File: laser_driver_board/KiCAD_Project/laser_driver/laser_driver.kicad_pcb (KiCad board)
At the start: 2 copper layers, 101.6 x 33 mm, 9 parts, among them J1 Input, J2 Output, U1 LD1255R

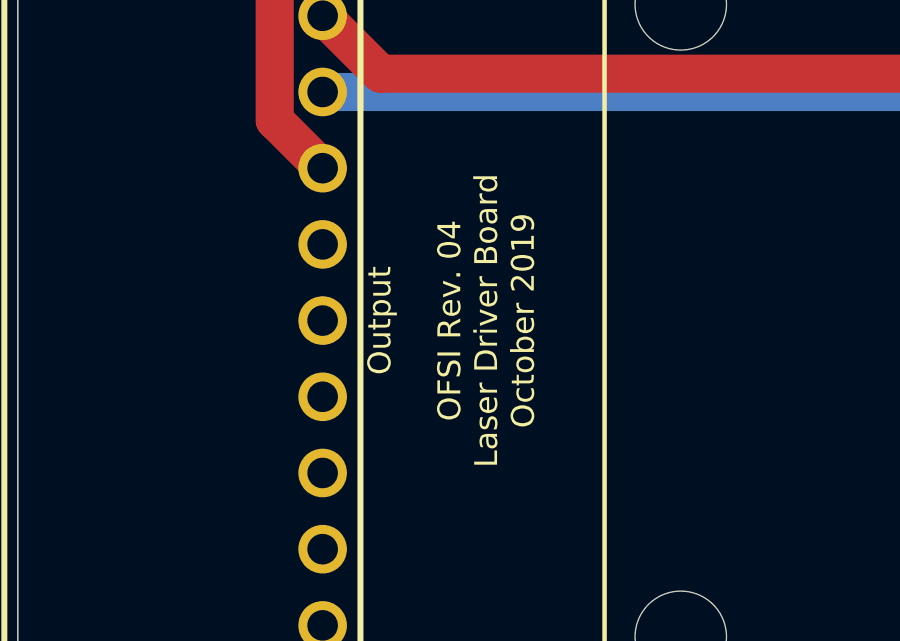
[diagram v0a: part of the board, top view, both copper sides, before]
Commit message: Change laser driver to OFMI
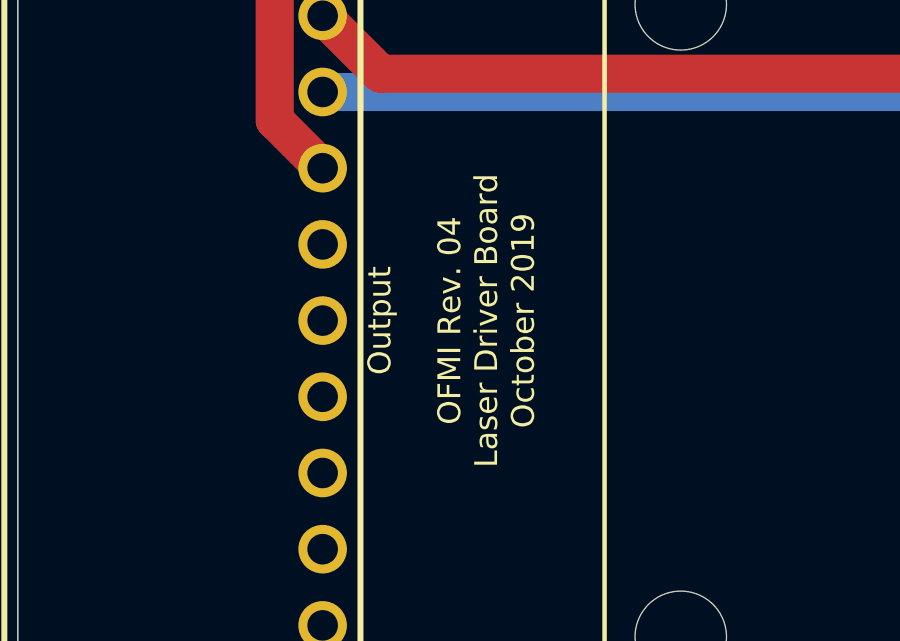
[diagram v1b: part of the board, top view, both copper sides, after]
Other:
- board text added: "OFMI Rev. 04 Laser Driver Board October 2019"
- board text removed: "OFSI Rev. 04 Laser Driver Board October 2019"
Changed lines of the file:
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@@
     (effects (font (size 0.762 0.762) (thickness 0.15)) (justify mirror))
   )
-  (gr_text "OFSI Rev. 04\nLaser Driver Board\nOctober 2019" (at 142.621 92.71 90) (layer F.SilkS)
+  (gr_text "OFMI Rev. 04\nLaser Driver Board\nOctober 2019" (at 142.621 92.71 90) (layer F.SilkS)
     (effects (font (size 0.762 0.762) (thickness 0.15)))
   )

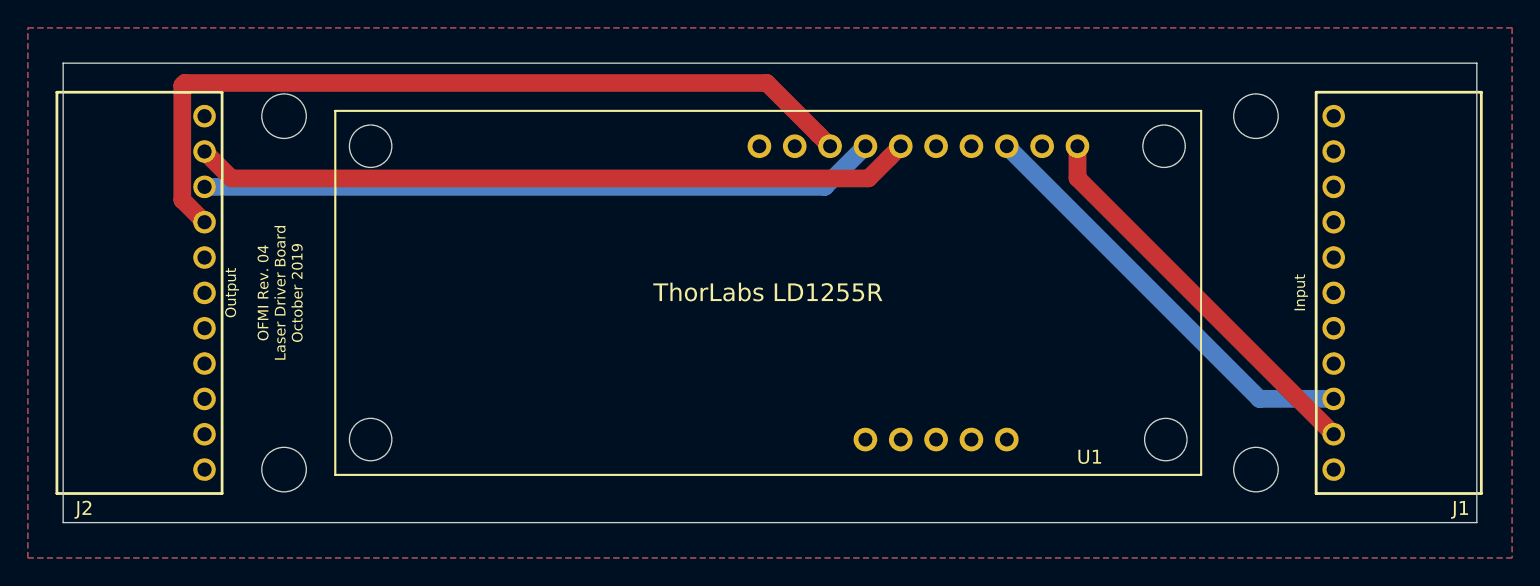
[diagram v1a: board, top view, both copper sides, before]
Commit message: Laser driver board rev 4.1 updates.
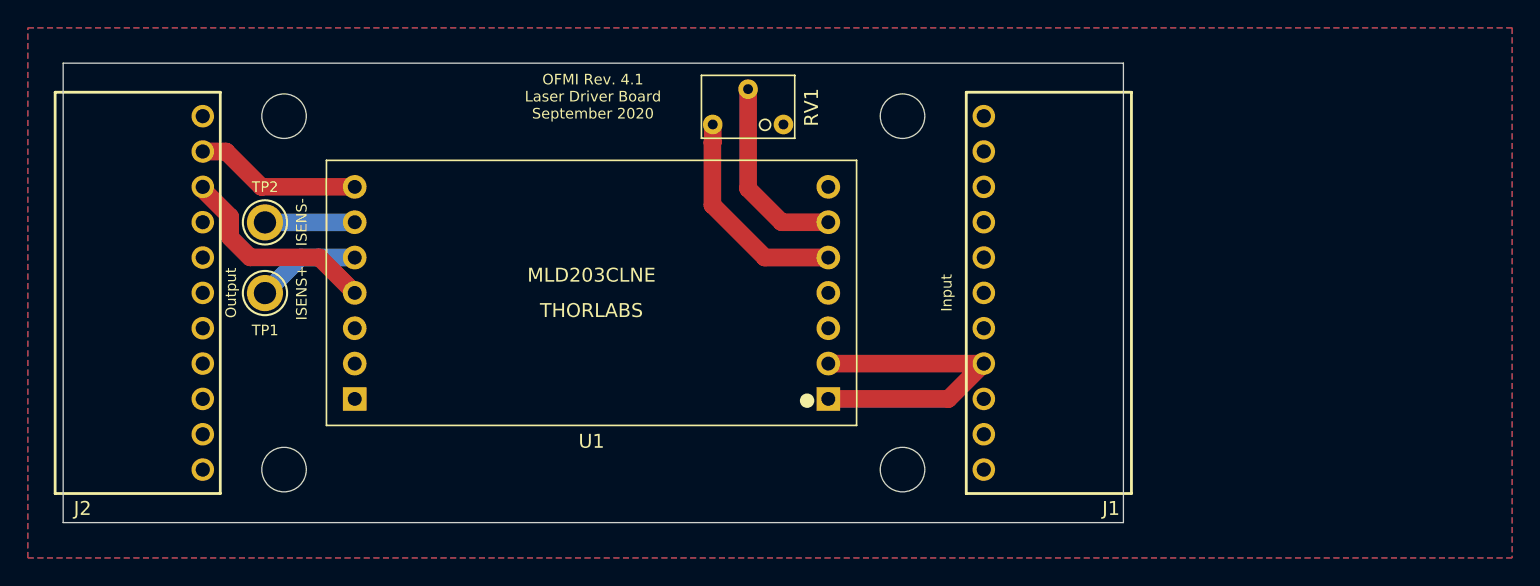
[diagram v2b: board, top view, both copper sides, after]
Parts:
- removed OB1, OB2: Test Point (on LD1255R), lib_fp:OffBoard
- added RV1: R_POT, lib_fp:3266W, F.Cu at (176.2, 79.3)
- added TP1: TestPoint, lib_fp:5006_TestPoint, F.Cu at (141.5, 92.7)
- added TP2: TestPoint, lib_fp:5006_TestPoint, F.Cu at (141.5, 87.6)
- U1: value LD1255R -> MLD203CLNE; footprint lib_fp:LD1255R -> lib_fp:MLD203CLN
- moved H3 25.4 mm to (187.3, 80.0)
- moved H4 25.4 mm to (187.3, 105.4)
- moved J1 25.1 mm to (196.2, 92.7)
- moved U1 12.7 mm to (165.0, 92.7)
- moved J2 0.13 mm to (134.0, 92.7)
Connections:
- J1 pad 2: +12V -> (no net)
- J1 pad 3: -12V -> (no net)
- J1 pad 4: (no net) -> +5V
- J2 pad 2: LDA -> /LDA
- J2 pad 3: LDC -> /LDC
- J2 pad 4: PDA -> (no net)
- U1 pad 1: +12V -> +5V
- U1 pad 11: (no net) -> /LDC
- U1 pad 12: (no net) -> /ISENS+
- U1 pad 13: (no net) -> /ISENS-
- U1 pad 14: (no net) -> /LDA
- U1 pad 2: GND -> +5V
- U1 pad 3: -12V -> GND
- U1 pad 4: (no net) -> GND
- U1 pad 5: (no net) -> Net-(RV1-Pad3)
- U1 pad 6: LDA -> /ISET
- U1 pad 7: LDC -> (no net)
- U1 pad 8: PDA -> (no net)
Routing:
- net PDA: track 59.0 -> 0.00 mm
- net LDA: track 51.8 -> 0.00 mm
- net LDC: track 48.7 -> 0.00 mm
- net -12V: track 31.0 -> 0.00 mm
- net +12V: track 28.3 -> 0.00 mm
- net +5V: track 0.00 -> 23.4 mm
- net Net-(RV1-Pad3): track 0.00 -> 15.7 mm
- net /LDC: track 0.00 -> 15.1 mm
- net /ISET: track 0.00 -> 13.9 mm
- net /LDA: track 0.00 -> 12.0 mm
- net /ISENS+: track 0.00 -> 7.51 mm
- net /ISENS-: track 0.00 -> 6.46 mm
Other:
- board size 101.6 x 33 mm -> 76.2 x 33 mm
- board text added: "+5V"
- board text added: "ISENS+"
- board text added: "ISENS-"
- board text added: "OFMI Rev. 4.1 Laser Driver Board September 2020"
- board text removed: "+12"
- board text removed: "-12"
- board text removed: "LG 3-0000015"
- board text removed: "OFMI Rev. 04 Laser Driver Board October 2019"
- board text removed: "PDA"
